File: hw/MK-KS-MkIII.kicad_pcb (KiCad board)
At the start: 2 copper layers, 104.1 x 78.7 mm, 81 parts, among them J1 MuKOB IF, J2 LOOP PWR, J3 KEY-PADDLE, J4 COMM-DCE-10, J5 RPi-GPIO40, J6 I2C Disp, Q1 G01N20LE, Q2 2N3904, Q3 2N3904, SW1 CLOSER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

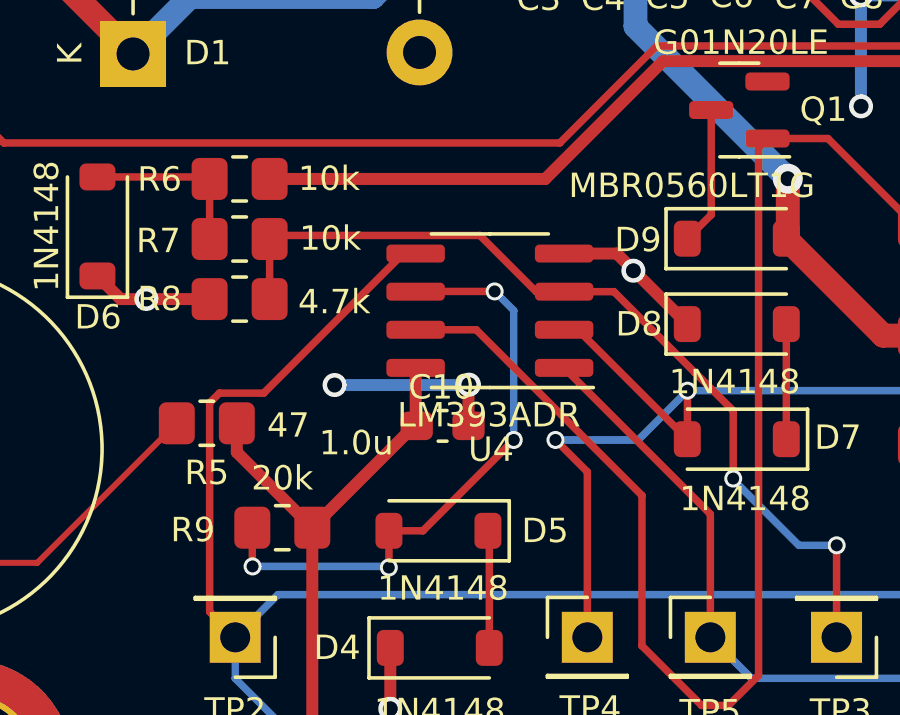
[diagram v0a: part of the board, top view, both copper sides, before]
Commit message: MK-IF-MKIII and JackAdapter PCBs produced.
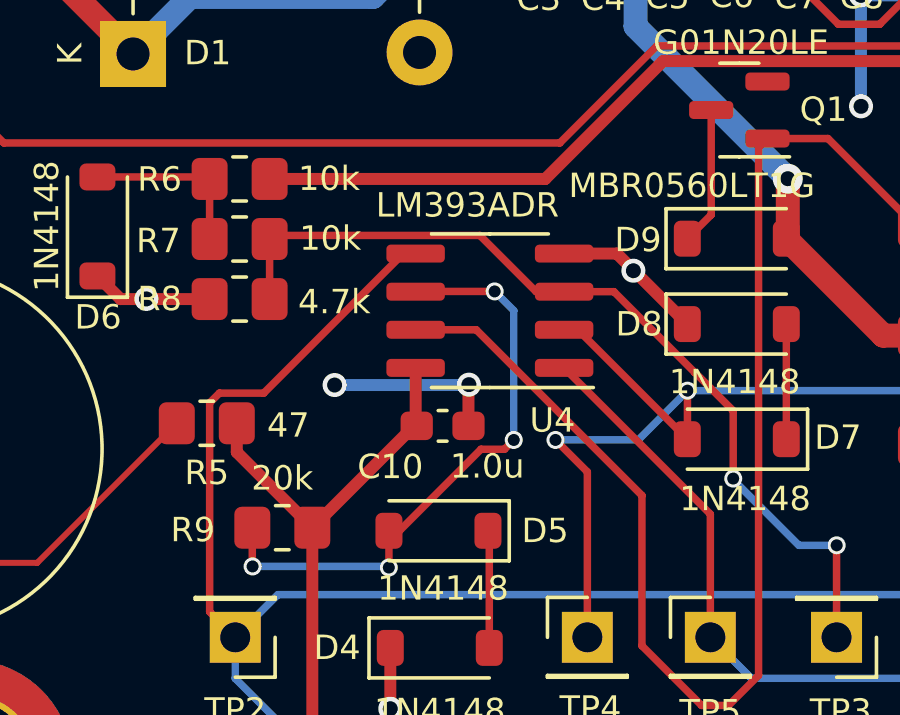
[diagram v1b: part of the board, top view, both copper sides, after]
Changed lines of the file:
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@@
     (title "MuKOB / RPi / USB - Key/Paddle&Sounder Interface MkIII")
     (date "2024-04-04")
-    (rev "1.0")
+    (rev "1.0b")
     (company "Silky Design AES")
     (comment 1 "Copyright AESilky 2023-24")
@@
     (property "ki_keywords" "cap capacitor")
     (attr smd)
-    (fp_text reference "C10" (at 0.046 1.287) (layer "F.SilkS")
+    (fp_text reference "C10" (at 1.744 -1.365) (layer "F.SilkS")
         (effects (font (size 0.8128 0.8128) (thickness 0.15)))
     )
-    (fp_text value "1.0u" (at 2.879 -0.572) (layer "F.SilkS")
+    (fp_text value "1.0u" (at -1.486 -1.348) (layer "F.SilkS")
         (effects (font (size 0.8128 0.8128) (thickness 0.15)))
     )
@@
     (property "Status" "Active")
     (attr smd)
-    (fp_text reference "U4" (at -0.039 -4.628) (layer "F.SilkS")
+    (fp_text reference "U4" (at -2.0864 -3.6538) (layer "F.SilkS")
         (effects (font (size 0.8128 0.8128) (thickness 0.15)))
     )
-    (fp_text value "LM393ADR" (at 0.0324 -3.4802) (layer "F.SilkS")
+    (fp_text value "LM393ADR" (at 0.7486 3.5162) (layer "F.SilkS")
         (effects (font (size 0.8128 0.8128) (thickness 0.15)))
     )
@@
   (segment (start 140.501 105.089) (end 137.2125 105.089) (width 0.4) (layer "F.Cu") (net 24))
   (segment (start 87.52 141.705) (end 87.52 137.846) (width 0.25) (layer "F.Cu") (net 25))
+  (segment (start 88.0254 135.0828) (end 88.3354 134.7728) (width 0.25) (layer "F.Cu") (net 26))
   (segment (start 84.1704 139.0258) (end 84.175 139.0212) (width 0.25) (layer "F.Cu") (net 26))
-  (segment (start 84.175 137.801) (end 85.3072 137.801) (width 0.25) (layer "F.Cu") (net 26))
+  (segment (start 84.175 137.801) (end 84.5252 137.801) (width 0.25) (layer "F.Cu") (net 26))
   (segment (start 79.62 137.698) (end 79.62 138.9794) (width 0.25) (layer "F.Cu") (net 26))
-  (segment (start 85.3072 137.801) (end 88.3354 134.7728) (width 0.25) (layer "F.Cu") (net 26))
+  (segment (start 87.2434 135.0828) (end 88.0254 135.0828) (width 0.25) (layer "F.Cu") (net 26))
   (segment (start 84.175 139.0212) (end 84.175 137.801) (width 0.25) (layer "F.Cu") (net 26))
   (segment (start 79.62 138.9794) (end 79.6294 138.9888) (width 0.25) (layer "F.Cu") (net 26))
+  (segment (start 84.5252 137.801) (end 87.2434 135.0828) (width 0.25) (layer "F.Cu") (net 26))
   (segment (start 87.6984 129.8218) (end 85.0722 129.8218) (width 0.25) (layer "F.Cu") (net 26))
   (via (at 88.3354 134.7728) (size 0.6) (drill 0.4) (layers "F.Cu" "B.Cu") (net 26))

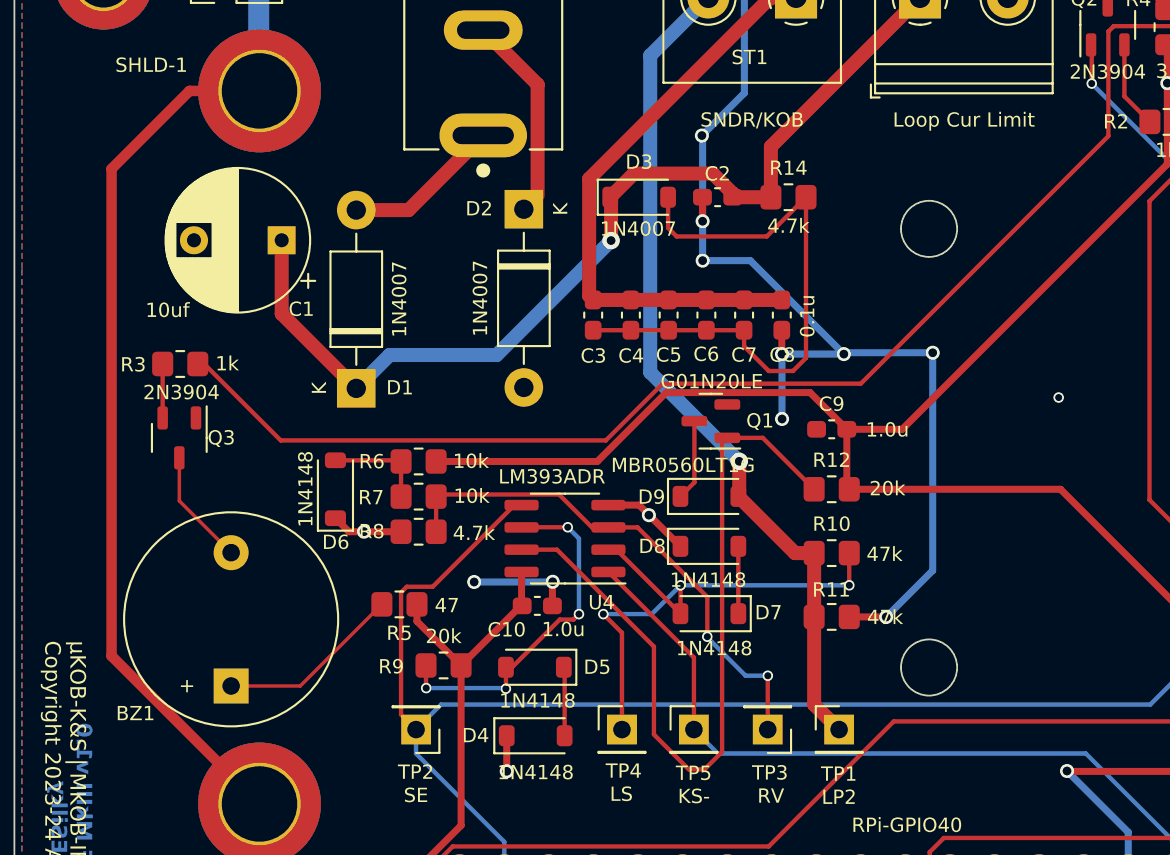
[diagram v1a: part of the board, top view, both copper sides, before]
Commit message: Update manual. Add IF-MkIV.
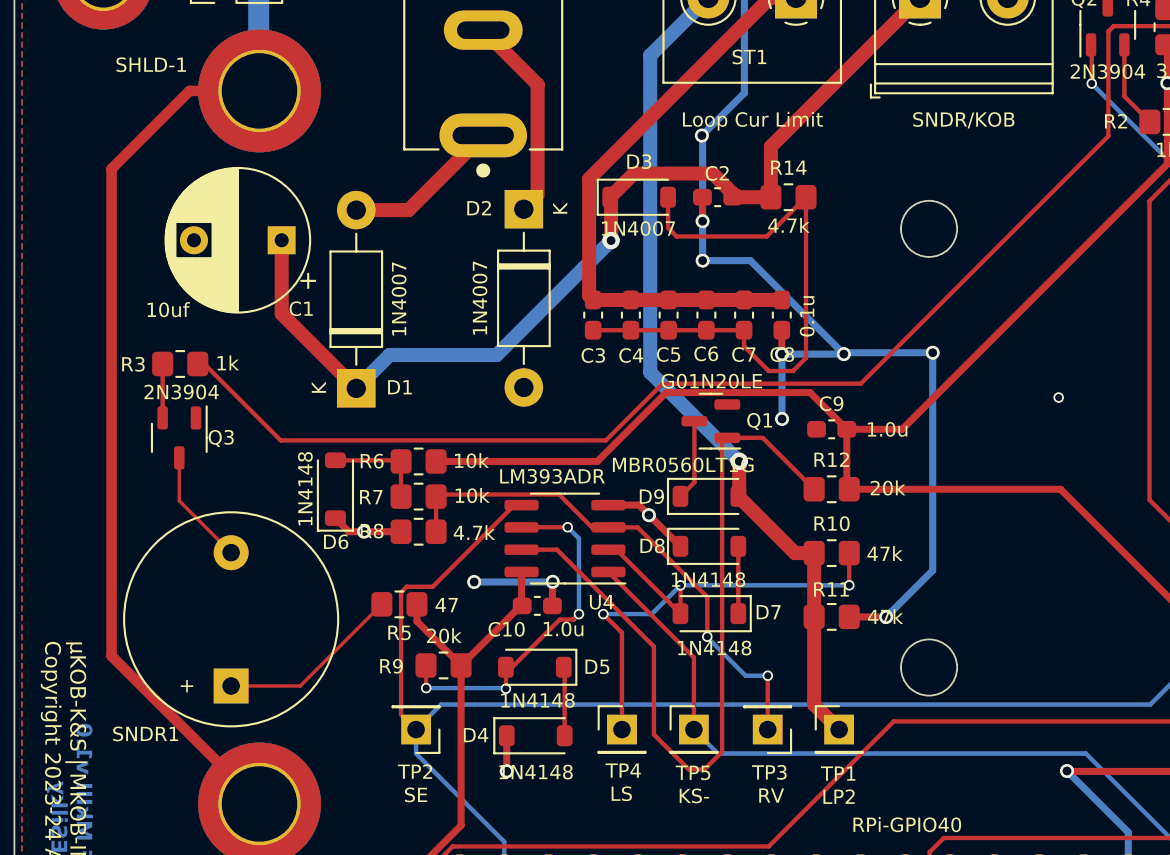
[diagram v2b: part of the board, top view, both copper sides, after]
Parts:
- ST1: value SNDR/KOB -> Loop Cur Limit
- ST2: value Loop Cur Limit -> SNDR/KOB
- renumbered BZ1 to SNDR1
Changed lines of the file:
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@@
   (title_block
     (title "MuKOB / RPi / USB - Key/Paddle&Sounder Interface MkIII")
-    (date "2024-04-04")
-    (rev "1.0b")
+    (date "2024-05-28")
+    (rev "1.0c")
     (company "Silky Design AES")
     (comment 1 "Copyright AESilky 2023-24")
@@
         (effects (font (size 0.8128 0.8128) (thickness 0.15)))
     )
-    (fp_text value "SNDR/KOB" (at 2.5 -6.985) (layer "F.SilkS")
+    (fp_text value "Loop Cur Limit" (at 2.5 -6.985) (layer "F.SilkS")
         (effects (font (size 0.8128 0.8128) (thickness 0.15)))
     )
@@
         (effects (font (size 0.8128 0.8128) (thickness 0.15)))
     )
-    (fp_text value "Loop Cur Limit" (at 2.5 6.985) (layer "F.SilkS")
+    (fp_text value "SNDR/KOB" (at 2.5 6.985) (layer "F.SilkS")
         (effects (font (size 0.8128 0.8128) (thickness 0.15)))
     )
@@
     (property "ki_keywords" "quartz resonator ceramic")
     (attr through_hole)
-    (fp_text reference "BZ1" (at -1.573 -5.45 180) (layer "F.SilkS")
+    (fp_text reference "SNDR1" (at -2.7618 -4.8566 180) (layer "F.SilkS")
         (effects (font (size 0.8128 0.8128) (thickness 0.15)))
     )
@@
     (pts (xy 56.1594 93.5228) (xy 160.2994 93.5228))
     (height -14.732)
-    (gr_text "104.1400 mm" (at 108.2294 77.6408) (layer "User.2")
+    (gr_text "4.1000 in" (at 108.2294 77.6408) (layer "User.2")
       (effects (font (size 1 1) (thickness 0.15)))
     )
@@
     (pts (xy 61.2394 98.6028) (xy 155.2194 98.6028))
     (height -15.24)
-    (gr_text "93.9800 mm" (at 108.2294 82.2128) (layer "User.2")
+    (gr_text "3.7000 in" (at 108.2294 82.2128) (layer "User.2")
       (effects (font (size 1 1) (thickness 0.15)))
     )
@@
     (pts (xy 146.3294 104.9528) (xy 146.3294 145.5928))
     (height -25.1076)
-    (gr_text "40.6400 mm" (at 170.287 125.2728 90) (layer "User.2")
+    (gr_text "1.6000 in" (at 170.287 125.2728 90) (layer "User.2")
       (effects (font (size 1 1) (thickness 0.15)))
     )
@@
     (pts (xy 155.2194 98.6028) (xy 155.2194 104.899))
     (height -16.2176)
-    (gr_text "6.2962 mm" (at 170.287 101.7509 90) (layer "User.2")
+    (gr_text "0.2479 in" (at 170.287 101.7509 90) (layer "User.2")
       (effects (font (size 1 1) (thickness 0.15)))
     )
@@
     (pts (xy 61.2394 98.6028) (xy 137.4394 98.6028))
     (height -10.16)
-    (gr_text "76.2000 mm" (at 99.3394 87.2928) (layer "User.2")
+    (gr_text "3.0000 in" (at 99.3394 87.2928) (layer "User.2")
       (effects (font (size 1 1) (thickness 0.15)))
     )
@@
     (pts (xy 61.2394 98.6028) (xy 61.2394 136.7028))
     (height 10.159999)
-    (gr_text "38.1000 mm" (at 49.929401 117.6528 90) (layer "User.2")
+    (gr_text "1.5000 in" (at 49.929401 117.6528 90) (layer "User.2")
       (effects (font (size 1 1) (thickness 0.15)))
     )
@@
     (pts (xy 70.1294 104.9528) (xy 146.3294 104.9528))
     (height -19.1788)
-    (gr_text "76.2000 mm" (at 108.2294 84.624) (layer "User.2")
+    (gr_text "3.0000 in" (at 108.2294 84.624) (layer "User.2")
       (effects (font (size 1 1) (thickness 0.15)))
     )
@@
     (pts (xy 61.2394 98.6028) (xy 61.2394 167.1828))
     (height 15.239999)
-    (gr_text "68.5800 mm" (at 44.849401 132.8928 90) (layer "User.2")
+    (gr_text "2.7000 in" (at 44.849401 132.8928 90) (layer "User.2")
       (effects (font (size 1 1) (thickness 0.15)))
     )
@@
     (pts (xy 61.2394 98.6028) (xy 70.1 98.6028))
     (height -12.8288)
-    (gr_text "8.8606 mm" (at 65.6697 84.624) (layer "User.2")
+    (gr_text "0.3488 in" (at 65.6697 84.624) (layer "User.2")
       (effects (font (size 1 1) (thickness 0.15)))
     )
@@
     (pts (xy 56.1594 93.5228) (xy 56.1594 172.2628))
     (height 15.24)
-    (gr_text "78.7400 mm" (at 39.7694 132.8928 90) (layer "User.2")
+    (gr_text "3.1000 in" (at 39.7694 132.8928 90) (layer "User.2")
       (effects (font (size 1 1) (thickness 0.15)))
     )
